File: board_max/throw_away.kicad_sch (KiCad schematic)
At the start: 21 parts, among them U1 MAX4820xUP, U2 MAX4820xUP, U3 MAX4820xUP, U4 MAX4820xUP, U5 MAX4820xUP, U6 ESP32-S3-DevKitC

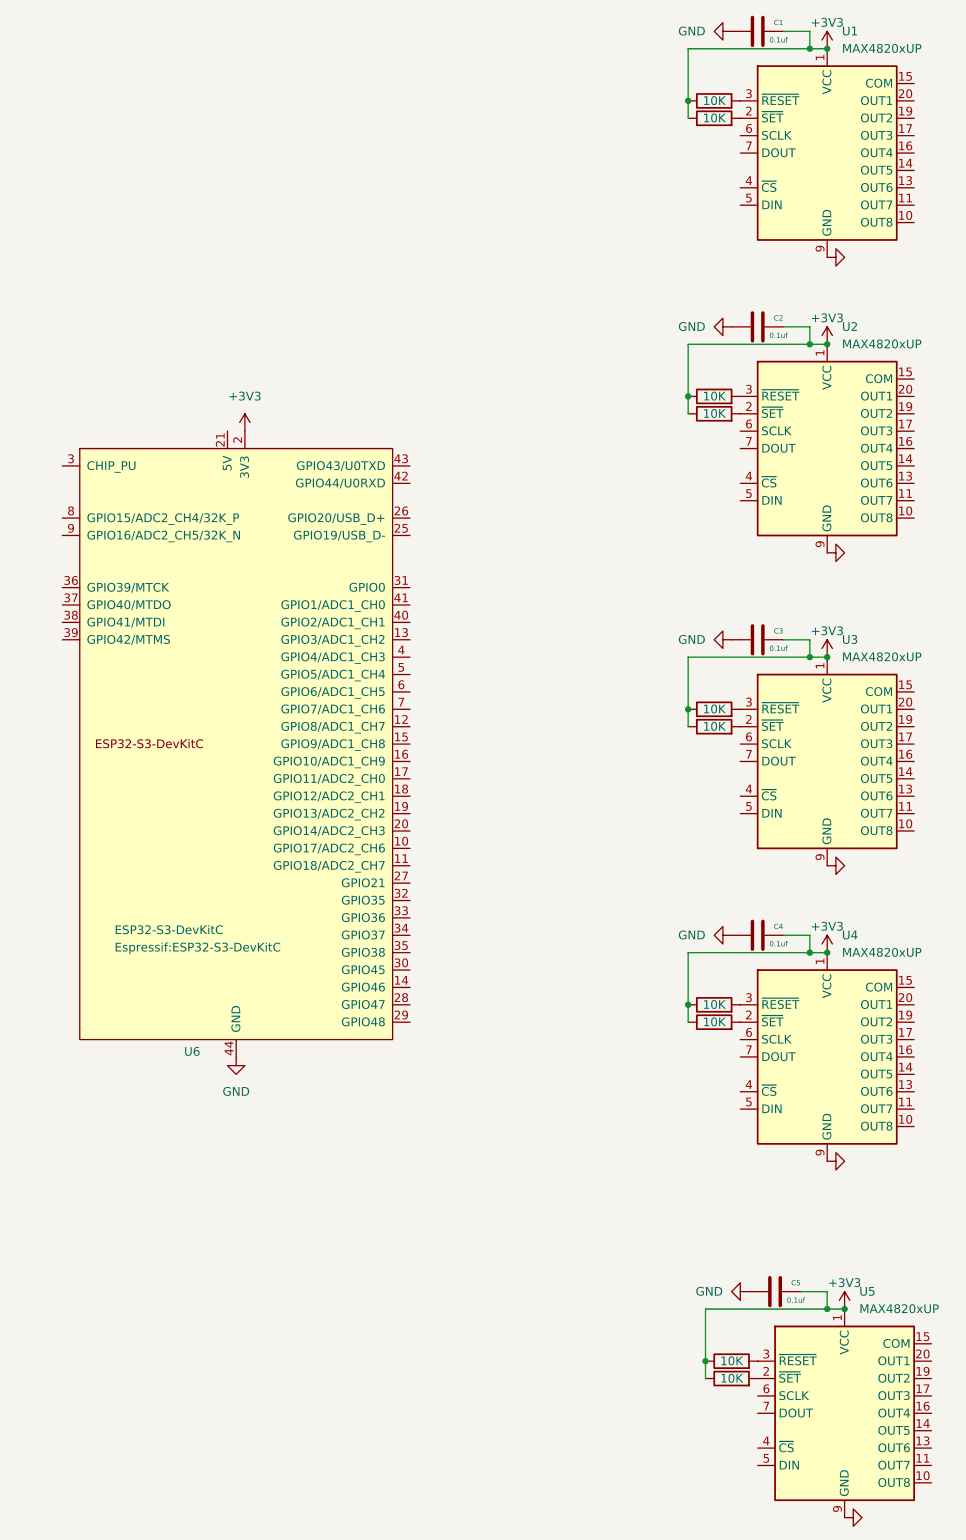
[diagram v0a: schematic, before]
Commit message: finished connecting max4820 chips to ESP32
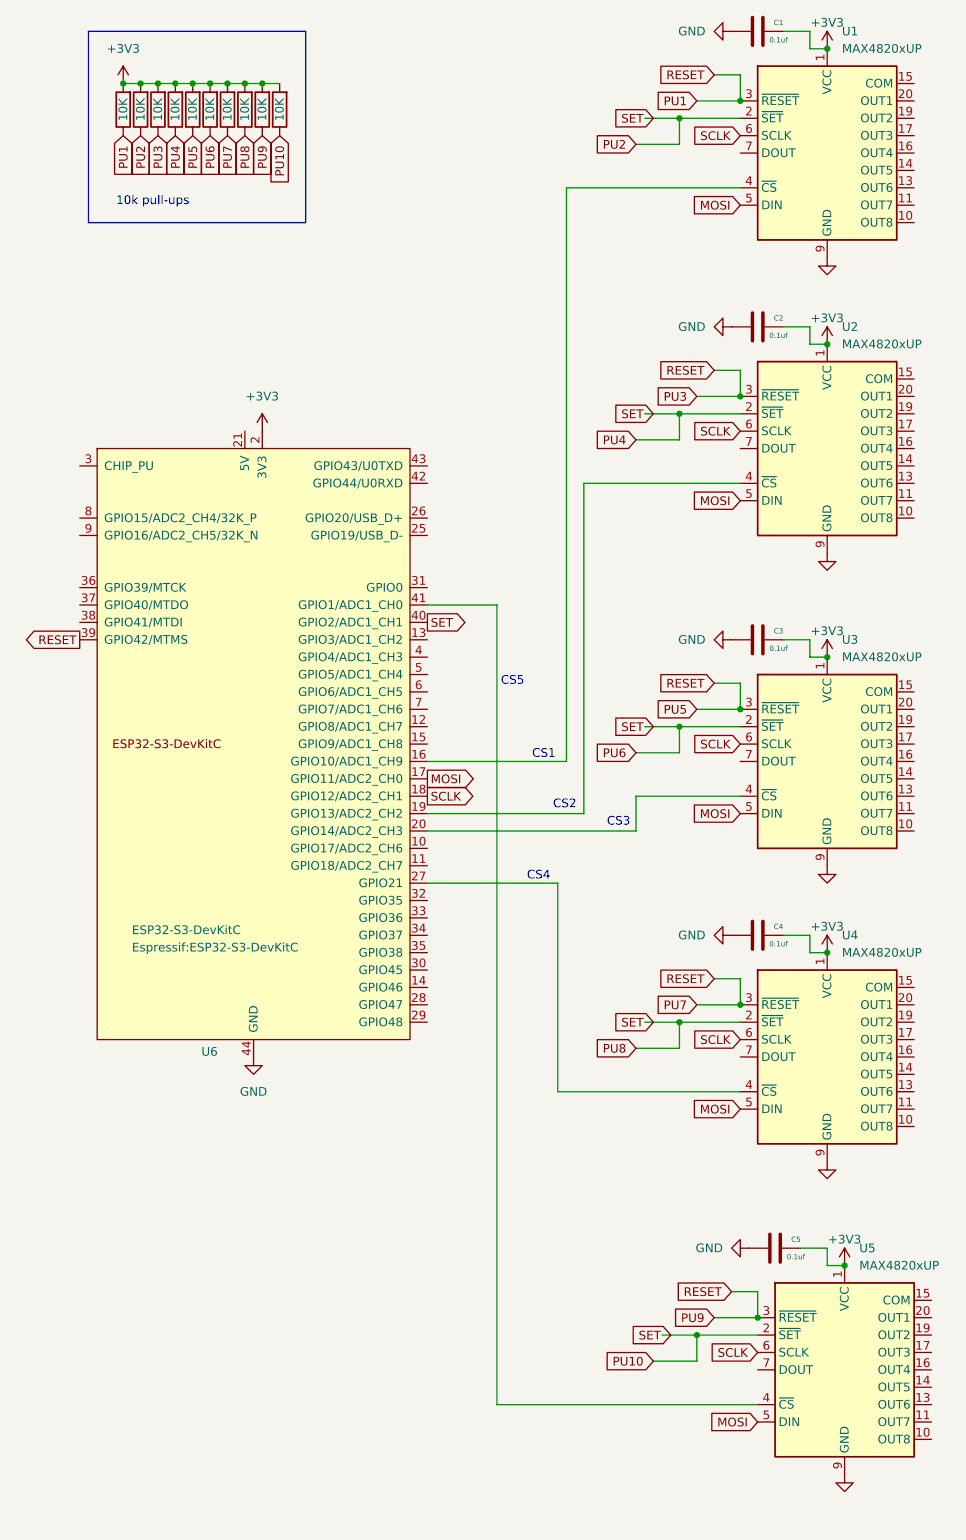
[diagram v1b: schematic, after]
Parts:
- removed R1, R10, R2, R3, R4, R5, R6, R7, R8, R9: 10K, Resistor_SMD:R_0805_2012Metric_Pad1.20x1.40mm_HandSolder, symbol Device:R
- added R11, R12, R13, R14, R15, R16, R17, R18, R19, R20: 10K, Resistor_SMD:R_0805_2012Metric_Pad1.20x1.40mm_HandSolder, symbol Device:R
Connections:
- net +3V3: now also R11.2, R12.2, R13.2, R14.2, R15.2, R16.2, R17.2, R18.2, R19.2, R20.2
- net PU10: now reaches U3.2 (~{SET})
- net PU10: now also U1.2 (~{SET}), U2.2 (~{SET}), U4.2 (~{SET}), U5.2 (~{SET}), U6.40 (GPIO2/ADC1_CH1), R12.1, R14.1, R16.1, R18.1, R20.1
- net PU1: now reaches U3.3 (~{RESET})
- net PU1: now also U1.3 (~{RESET}), U2.3 (~{RESET}), U4.3 (~{RESET}), U5.3 (~{RESET}), U6.39 (GPIO42/MTMS), R11.1, R13.1, R15.1, R17.1, R19.1
- net at U3.4 (~{CS}): now also U6.20 (GPIO14/ADC2_CH3)
- net MOSI: now reaches U3.5 (DIN)
- net MOSI: now also U1.5 (DIN), U2.5 (DIN), U4.5 (DIN), U5.5 (DIN), U6.17 (GPIO11/ADC2_CH0)
- net SCLK: now reaches U3.6 (SCLK)
- net SCLK: now also U1.6 (SCLK), U2.6 (SCLK), U4.6 (SCLK), U5.6 (SCLK), U6.18 (GPIO12/ADC2_CH1)
- net at U1.4 (~{CS}): now also U6.16 (GPIO10/ADC1_CH9)
- net at U5.4 (~{CS}): now also U6.41 (GPIO1/ADC1_CH0)
- net at U2.4 (~{CS}): now also U6.19 (GPIO13/ADC2_CH2)
- net at U4.4 (~{CS}): now also U6.27 (GPIO21)
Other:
- note added: "10k pull-ups"
- note added: "CS1"
- note added: "CS2"
- note added: "CS3"
- note added: "CS4"
- note added: "CS5"
- moved on the sheet: C5, U5, U6

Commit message: We added dual operating mode support to the GAP Tuner: Field mode (AP) is now a first-class operating mode stored in NVS flash alongside Home WiFi mode, with NetworkMgr refactored to drop   its own web server and WebServerManager taking sole ownership of all HTTP routing in both modes. A gear icon on the main tuner page links to a new /settings page where the user can toggle   between modes — displaying AP credentials in field mode and a pre-populated WiFi credential form in home mode — with the Apply & Restart button disabled until something actually changes,   context-sensitive status copy ("X mode is active" vs "Switch to X mode"), and post-save instructions that include a 20-second countdown redirect to gaptuner.local when switching to home   mode, using an AbortController timeout to ensure the instructions appear even when the device restarts before the HTTP response is delivered.
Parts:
- removed C3: 0.1uf, C_0805_2012Metric_Pad1.18x1.45mm_HandSolder, symbol Device:C
- added K1: EE2-3NU, Relay_SMD:Relay_DPDT_Kemet_EE2_NU, symbol Relay:EE2-3NU
- added K2, K3, K4, K5, K6, K7, K8, K9: EE2-3TNU, Relay_SMD:Relay_DPDT_Kemet_EE2_NU_DoubleCoil, symbol Relay:EE2-3TNU
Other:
- moved on the sheet: C2
